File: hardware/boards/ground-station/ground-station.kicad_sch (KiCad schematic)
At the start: 10 parts, among them J101 Raspberry_Pi_2_3, J102 Conn_01x15, J5 Conn_01x12

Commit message: Added footprints for most things
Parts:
- J102: footprint (none) -> capstone:CON15_1X15_DRB_SFW; Part No. (none) -> SFW15R-1STE1LF
- J5: footprint (none) -> Connector_PinHeader_2.54mm:PinHeader_1x12_P2.54mm_Vertical
- R101, R102: footprint (none) -> Resistor_SMD:R_0201_0603Metric
- R23, R24, R25, R26: footprint (none) -> Resistor_SMD:R_0402_1005Metric
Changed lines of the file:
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@@
       (effects (font (size 1.27 1.27)))
     )
-    (property "Footprint" "" (at 220.98 122.555 0)
+    (property "Footprint" "Resistor_SMD:R_0402_1005Metric" (at 220.98 122.555 0)
       (effects (font (size 1.27 1.27)) hide)
     )
@@
       (effects (font (size 1.27 1.27)))
     )
-    (property "Footprint" "" (at 220.98 112.395 0)
+    (property "Footprint" "Resistor_SMD:R_0402_1005Metric" (at 220.98 112.395 0)
       (effects (font (size 1.27 1.27)) hide)
     )
@@
       (effects (font (size 1.27 1.27)) (justify left))
     )
-    (property "Footprint" "" (at 265.43 40.64 0)
+    (property "Footprint" "Connector_PinHeader_2.54mm:PinHeader_1x12_P2.54mm_Vertical" (at 265.43 40.64 0)
       (effects (font (size 1.27 1.27)) hide)
     )
     (property "Datasheet" "~" (at 265.43 40.64 0)
-      (effects (font (size 1.27 1.27)) hide)
-    )
-    (pin "5")
-    (pin "6")
-    (pin "7")
-    (pin "8")
-    (pin "1")
-    (pin "9")
-    (pin "3")
-    (pin "10")
-    (pin "11")
-    (pin "2")
-    (pin "12")
-    (pin "4")
-    (instances
-      (project "ground-station"
-        (path "/ce329892-de08-4d39-b253-15f3aaf1c085"
-          (reference "J5") (unit 1)
-        )
-      )
-    )
-  )
-  (symbol (lib_id "Device:R_Small_US") (at 128.905 34.29 180) (unit 1)
-    (in_bom yes) (on_board yes) (dnp no) (fields_autoplaced)
-    (property "Reference" "R102" (at 131.445 33.02 0)
-      (effects (font (size 1.27 1.27)) (justify right))
-    )
-    (property "Value" "4.7k" (at 131.445 35.56 0)
-      (effects (font (size 1.27 1.27)) (justify right))
-    )
-    (property "Footprint" "" (at 128.905 34.29 0)
-      (effects (font (size 1.27 1.27)) hide)
-    )
-    (property "Datasheet" "~" (at 128.905 34.29 0)
-      (effects (font (size 1.27 1.27)) hide)
-    )
-    (pin "1")
-    (pin "2")
-    (instances
-      (project "ground-station"
-        (path "/ce329892-de08-4d39-b253-15f3aaf1c085"
-          (reference "R102") (unit 1)
-        )
-      )
-    )
-  )
-  (symbol (lib_id "Device:R_Small_US") (at 120.015 34.29 180) (unit 1)
-    (in_bom yes) (on_board yes) (dnp no) (fields_autoplaced)
-    (property "Reference" "R101" (at 121.92 33.02 0)
-      (effects (font (size 1.27 1.27)) (justify right))
-    )
-    (property "Value" "4.7k" (at 121.92 35.56 0)
-      (effects (font (size 1.27 1.27)) (justify right))
-    )
-    (property "Footprint" "" (at 120.015 34.29 0)
-      (effects (font (size 1.27 1.27)) hide)
-    )
-    (property "Datasheet" "~" (at 120.015 34.29 0)
-      (effects (font (size 1.27 1.27)) hide)
-    )
-    (pin "1")
-    (pin "2")
-    (instances
-      (project "ground-station"
-        (path "/ce329892-de08-4d39-b253-15f3aaf1c085"
-          (reference "R101") (unit 1)
-        )
-      )
-    )
-  )
-  (symbol (lib_id "power:GND") (at 257.81 57.15 0) (unit 1)
-    (in_bom yes) (on_board yes) (dnp no)
-    (property "Reference" "#PWR06" (at 257.81 63.5 0)
-      (effects (font (size 1.27 1.27)) hide)
-    )
-    (property "Value" "GND" (at 257.81 60.96 0)
-      (effects (font (size 1.27 1.27)))
-    )
-    (property "Footprint" "" (at 257.81 57.15 0)
-      (effects (font (size 1.27 1.27)) hide)
-    )
-    (property "Datasheet" "" (at 257.81 57.15 0)
-      (effects (font (size 1.27 1.27)) hide)
-    )
-    (pin "1")
-    (instances
-      (project "ground-station"
-        (path "/ce329892-de08-4d39-b253-15f3aaf1c085"
-          (reference "#PWR06") (unit 1)
-        )
-      )
-    )
-  )
-  (symbol (lib_id "Device:R_Small") (at 220.98 114.935 90) (unit 1)
-    (in_bom yes) (on_board yes) (dnp no)
-    (property "Reference" "R26" (at 217.805 114.3 90)
-      (effects (font (size 1.27 1.27)))
-    )
-    (property "Value" "0" (at 223.52 114.3 90)
-      (effects (font (size 1.27 1.27)))
-    )
-    (property "Footprint" "" (at 220.98 114.935 0)
-      (effects (font (size 1.27 1.27)) hide)
-    )
-    (property "Datasheet" "~" (at 220.98 114.935 0)
-      (effects (font (size 1.27 1.27)) hide)
-    )
-    (pin "1")
-    (pin "2")
-    (instances
-      (project "ground-station"
-        (path "/ce329892-de08-4d39-b253-15f3aaf1c085"
-          (reference "R26") (unit 1)
-        )
-      )
-    )
-  )
-  (symbol (lib_id "Connector_Generic:Conn_01x15") (at 245.745 127.635 0) (unit 1)
-    (in_bom yes) (on_board yes) (dnp no) (fields_autoplaced)
-    (property "Reference" "J102" (at 245.745 103.505 0)
-      (effects (font (size 1.27 1.27)))
-    )
-    (property "Value" "Conn_01x15" (at 245.745 106.045 0)
-      (effects (font (size 1.27 1.27)))
-    )
-    (property "Footprint" "" (at 245.745 127.635 0)
-      (effects (font (size 1.27 1.27)) hide)
-    )
-    (property "Datasheet" "~" (at 245.745 127.635 0)
       (effects (font (size 1.27 1.27)) hide)
     )
@@
     (pin "11")
     (pin "12")
-    (pin "13")
-    (pin "14")
-    (pin "15")
     (pin "2")
     (pin "3")
@@
       (project "ground-station"
         (path "/ce329892-de08-4d39-b253-15f3aaf1c085"
+          (reference "J5") (unit 1)
+        )
+      )
+    )
+  )
+  (symbol (lib_id "Device:R_Small_US") (at 128.905 34.29 180) (unit 1)
+    (in_bom yes) (on_board yes) (dnp no) (fields_autoplaced)
+    (property "Reference" "R102" (at 131.445 33.02 0)
+      (effects (font (size 1.27 1.27)) (justify right))
+    )
+    (property "Value" "4.7k" (at 131.445 35.56 0)
+      (effects (font (size 1.27 1.27)) (justify right))
+    )
+    (property "Footprint" "Resistor_SMD:R_0201_0603Metric" (at 128.905 34.29 0)
+      (effects (font (size 1.27 1.27)) hide)
+    )
+    (property "Datasheet" "~" (at 128.905 34.29 0)
+      (effects (font (size 1.27 1.27)) hide)
+    )
+    (pin "1")
+    (pin "2")
+    (instances
+      (project "ground-station"
+        (path "/ce329892-de08-4d39-b253-15f3aaf1c085"
+          (reference "R102") (unit 1)
+        )
+      )
+    )
+  )
+  (symbol (lib_id "Device:R_Small_US") (at 120.015 34.29 180) (unit 1)
+    (in_bom yes) (on_board yes) (dnp no) (fields_autoplaced)
+    (property "Reference" "R101" (at 121.92 33.02 0)
+      (effects (font (size 1.27 1.27)) (justify right))
+    )
+    (property "Value" "4.7k" (at 121.92 35.56 0)
+      (effects (font (size 1.27 1.27)) (justify right))
+    )
+    (property "Footprint" "Resistor_SMD:R_0201_0603Metric" (at 120.015 34.29 0)
+      (effects (font (size 1.27 1.27)) hide)
+    )
+    (property "Datasheet" "~" (at 120.015 34.29 0)
+      (effects (font (size 1.27 1.27)) hide)
+    )
+    (pin "1")
+    (pin "2")
+    (instances
+      (project "ground-station"
+        (path "/ce329892-de08-4d39-b253-15f3aaf1c085"
+          (reference "R101") (unit 1)
+        )
+      )
+    )
+  )
+  (symbol (lib_id "power:GND") (at 257.81 57.15 0) (unit 1)
+    (in_bom yes) (on_board yes) (dnp no)
+    (property "Reference" "#PWR06" (at 257.81 63.5 0)
+      (effects (font (size 1.27 1.27)) hide)
+    )
+    (property "Value" "GND" (at 257.81 60.96 0)
+      (effects (font (size 1.27 1.27)))
+    )
+    (property "Footprint" "" (at 257.81 57.15 0)
+      (effects (font (size 1.27 1.27)) hide)
+    )
+    (property "Datasheet" "" (at 257.81 57.15 0)
+      (effects (font (size 1.27 1.27)) hide)
+    )
+    (pin "1")
+    (instances
+      (project "ground-station"
+        (path "/ce329892-de08-4d39-b253-15f3aaf1c085"
+          (reference "#PWR06") (unit 1)
+        )
+      )
+    )
+  )
+  (symbol (lib_id "Device:R_Small") (at 220.98 114.935 90) (unit 1)
+    (in_bom yes) (on_board yes) (dnp no)
+    (property "Reference" "R26" (at 217.805 114.3 90)
+      (effects (font (size 1.27 1.27)))
+    )
+    (property "Value" "0" (at 223.52 114.3 90)
+      (effects (font (size 1.27 1.27)))
+    )
+    (property "Footprint" "Resistor_SMD:R_0402_1005Metric" (at 220.98 114.935 0)
+      (effects (font (size 1.27 1.27)) hide)
+    )
+    (property "Datasheet" "~" (at 220.98 114.935 0)
+      (effects (font (size 1.27 1.27)) hide)
+    )
+    (pin "1")
+    (pin "2")
+    (instances
+      (project "ground-station"
+        (path "/ce329892-de08-4d39-b253-15f3aaf1c085"
+          (reference "R26") (unit 1)
+        )
+      )
+    )
+  )
+  (symbol (lib_id "Connector_Generic:Conn_01x15") (at 245.745 127.635 0) (unit 1)
+    (in_bom yes) (on_board yes) (dnp no) (fields_autoplaced)
+    (property "Reference" "J102" (at 245.745 103.505 0)
+      (effects (font (size 1.27 1.27)))
+    )
+    (property "Value" "Conn_01x15" (at 245.745 106.045 0)
+      (effects (font (size 1.27 1.27)))
+    )
+    (property "Footprint" "capstone:CON15_1X15_DRB_SFW" (at 245.745 127.635 0)
+      (effects (font (size 1.27 1.27)) hide)
+    )
+    (property "Datasheet" "https://cdn.amphenol-cs.com/media/wysiwyg/files/drawing/sfw12lf.pdf" (at 245.745 127.635 0)
+      (effects (font (size 1.27 1.27)) hide)
+    )
+    (property "Part No." "SFW15R-1STE1LF" (at 245.745 127.635 0)
+      (effects (font (size 1.27 1.27)) hide)
+    )
+    (pin "1")
+    (pin "10")
+    (pin "11")
+    (pin "12")
+    (pin "13")
+    (pin "14")
+    (pin "15")
+    (pin "2")
+    (pin "3")
+    (pin "4")
+    (pin "5")
+    (pin "6")
+    (pin "7")
+    (pin "8")
+    (pin "9")
+    (instances
+      (project "ground-station"
+        (path "/ce329892-de08-4d39-b253-15f3aaf1c085"
           (reference "J102") (unit 1)
         )
@@
       (effects (font (size 1.27 1.27)) hide)
     )
-    (pin "2")
-    (pin "1")
+    (pin "1")
+    (pin "2")
     (instances
       (project "ground-station"
@@
       (effects (font (size 1.27 1.27)))
     )
-    (property "Footprint" "" (at 220.98 120.015 0)
-      (effects (font (size 1.27 1.27)) hide)
-    )
+    (property "Footprint" "Resistor_SMD:R_0402_1005Metric" (at 220.98 120.015 0)
+      (effects (font (size 1.27 1.27)) hide)
+    )

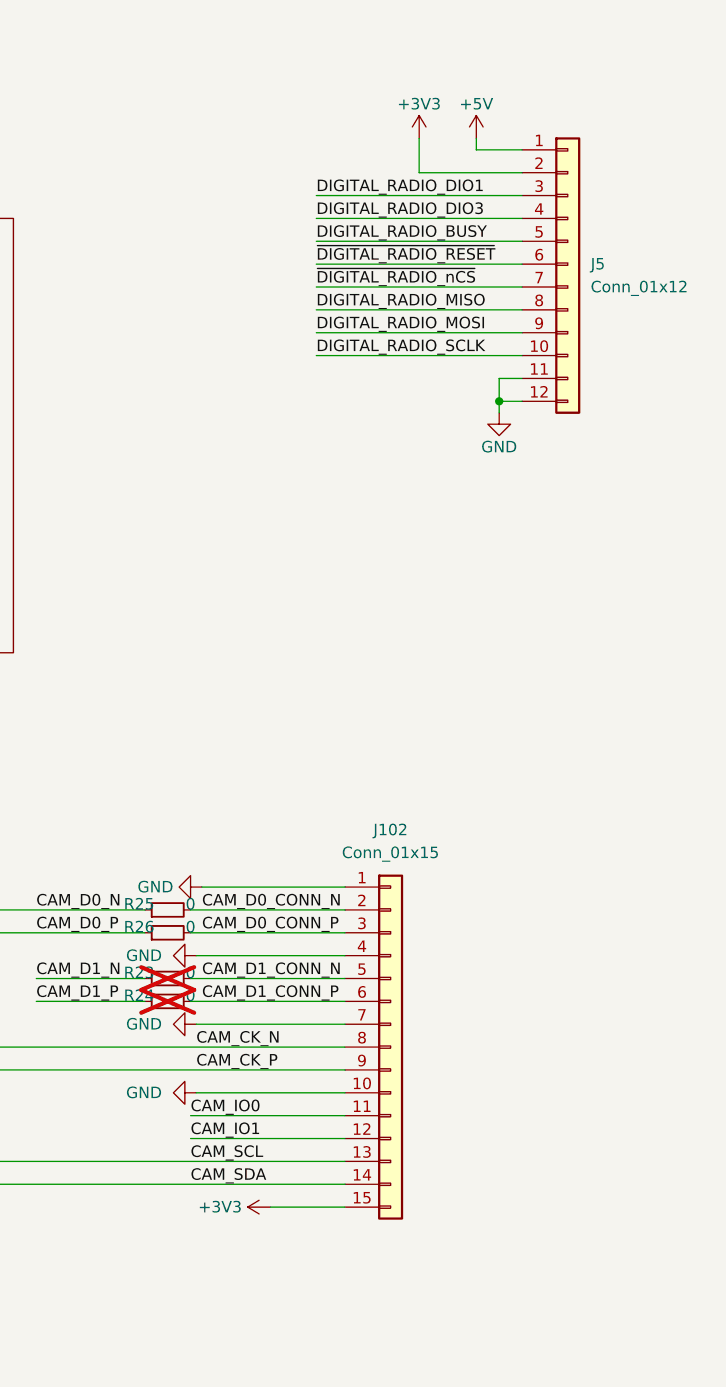
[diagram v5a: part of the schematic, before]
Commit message: Removed 10 pin radio header and changed ribbon cable connector
- disconnected 3V3 from the ribbon cable connector to keep the Pi 3V3 rail separate from the board 3V3 rail
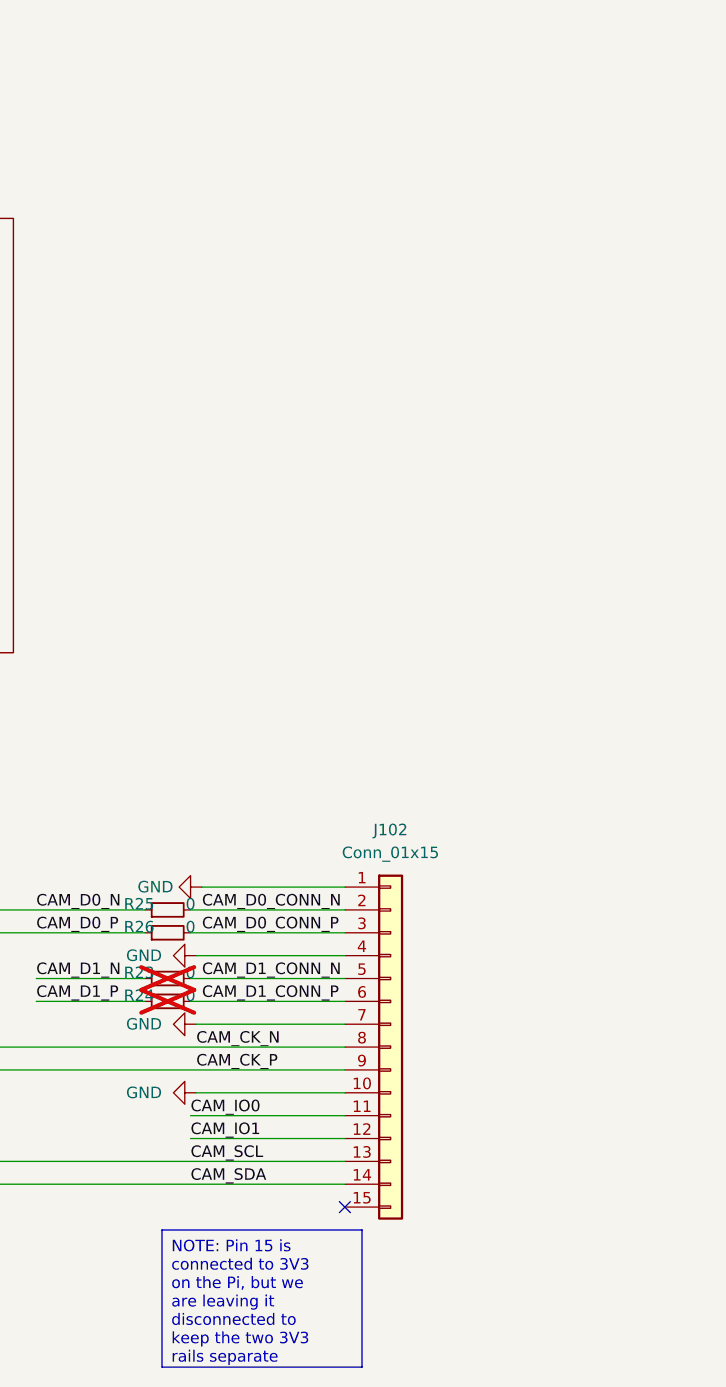
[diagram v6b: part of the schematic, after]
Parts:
- removed J5: Conn_01x12, Connector_PinHeader_2.54mm:PinHeader_1x12_P2.54mm_Vertical, symbol Connector_Generic:Conn_01x12
- J102: footprint capstone:CON15_1X15_DRB_SFW -> capstone:FFC3A20-15-G; Part No. SFW15R-1STE1LF -> FFC3A20-15-G
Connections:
- net +3V3: no longer J102.15 (Pin_15)
- no-connect marks 2 -> 3

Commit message: layout
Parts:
- removed R101, R102: 4.7k, Resistor_SMD:R_0201_0603Metric, symbol Device:R_Small_US
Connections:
- net CAM_D1_N is gone; now on net CAM_D0_N: R23.1
- net CAM_D1_P is gone; now on net CAM_D0_P: R24.1
- net I2C_SCL: no longer names the net of J101.5 (SCL/GPIO3)
- net I2C_SDA: no longer names the net of J101.3 (SDA/GPIO2)
- no-connect marks 3 -> 7
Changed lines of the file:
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@@
   (junction (at 79.375 91.44) (diameter 0) (color 0 0 0 0)
   )
+  (junction (at 205.105 112.395) (diameter 0) (color 0 0 0 0)
+  )
+  (junction (at 202.565 114.935) (diameter 0) (color 0 0 0 0)
+  )
   (junction (at 84.455 91.44) (diameter 0) (color 0 0 0 0)
   )
@@
   (junction (at 89.535 91.44) (diameter 0) (color 0 0 0 0)
   )
-  (junction (at 124.46 26.67) (diameter 0) (color 0 0 0 0)
-  )
   (junction (at 86.995 91.44) (diameter 0) (color 0 0 0 0)
   )
+  (no_connect (at 104.775 43.815))
   (no_connect (at 89.535 23.495))
+  (no_connect (at 104.775 41.275))
   (no_connect (at 86.995 23.495))
   (no_connect (at 240.665 145.415))
+  (no_connect (at 104.775 33.655))
+  (no_connect (at 104.775 36.195))
   (wire (pts (xy 86.995 91.44) (xy 84.455 91.44))
     (stroke (width 0) (type default))
@@
     (stroke (width 0) (type default))
   )
-  (wire (pts (xy 120.015 31.75) (xy 120.015 26.67))
-    (stroke (width 0) (type default))
-  )
-  (wire (pts (xy 104.775 43.815) (xy 128.905 43.815))
-    (stroke (width 0) (type default))
-  )
   (wire (pts (xy 45.085 64.135) (xy 64.135 64.135))
     (stroke (width 0) (type default))
@@
     (stroke (width 0) (type default))
   )
+  (wire (pts (xy 205.105 112.395) (xy 218.44 112.395))
+    (stroke (width 0) (type default))
+  )
   (wire (pts (xy 166.37 130.175) (xy 240.665 130.175))
     (stroke (width 0) (type default))
@@
     (stroke (width 0) (type default))
   )
-  (wire (pts (xy 197.485 112.395) (xy 218.44 112.395))
+  (wire (pts (xy 197.485 112.395) (xy 205.105 112.395))
     (stroke (width 0) (type default))
   )
@@
     (stroke (width 0) (type default))
   )
-  (wire (pts (xy 120.015 41.275) (xy 104.775 41.275))
-    (stroke (width 0) (type default))
-  )
   (wire (pts (xy 81.915 89.535) (xy 81.915 91.44))
     (stroke (width 0) (type default))
@@
     (stroke (width 0) (type default))
   )
-  (wire (pts (xy 218.44 120.015) (xy 206.375 120.015))
+  (wire (pts (xy 205.105 120.015) (xy 218.44 120.015))
     (stroke (width 0) (type default))
   )
@@
     (stroke (width 0) (type default))
   )
+  (wire (pts (xy 202.565 114.935) (xy 218.44 114.935))
+    (stroke (width 0) (type default))
+  )
   (wire (pts (xy 240.665 132.715) (xy 224.155 132.715))
     (stroke (width 0) (type default))
   )
-  (wire (pts (xy 218.44 122.555) (xy 206.375 122.555))
+  (wire (pts (xy 202.565 122.555) (xy 218.44 122.555))
     (stroke (width 0) (type default))
   )
@@
     (stroke (width 0) (type default))
   )
-  (wire (pts (xy 197.485 114.935) (xy 218.44 114.935))
+  (wire (pts (xy 197.485 114.935) (xy 202.565 114.935))
     (stroke (width 0) (type default))
   )
@@
     (stroke (width 0) (type default))
   )
-  (wire (pts (xy 128.905 31.75) (xy 128.905 26.67))
-    (stroke (width 0) (type default))
-  )
   (wire (pts (xy 240.665 125.095) (xy 224.155 125.095))
     (stroke (width 0) (type default))
@@
     (stroke (width 0) (type default))
   )
+  (wire (pts (xy 202.565 122.555) (xy 202.565 114.935))
+    (stroke (width 0) (type default))
+  )
   (wire (pts (xy 50.165 36.195) (xy 64.135 36.195))
     (stroke (width 0) (type default))
@@
     (stroke (width 0) (type default))
   )
-  (wire (pts (xy 120.015 36.83) (xy 120.015 41.275))
-    (stroke (width 0) (type default))
-  )
   (wire (pts (xy 156.21 140.335) (xy 240.665 140.335))
     (stroke (width 0) (type default))
   )
-  (wire (pts (xy 128.905 26.67) (xy 124.46 26.67))
-    (stroke (width 0) (type default))
-  )
   (wire (pts (xy 72.39 21.59) (xy 68.58 21.59))
     (stroke (width 0) (type default))
@@
     (stroke (width 0) (type default))
   )
+  (wire (pts (xy 205.105 120.015) (xy 205.105 112.395))
+    (stroke (width 0) (type default))
+  )
   (wire (pts (xy 86.995 89.535) (xy 86.995 91.44))
     (stroke (width 0) (type default))
@@
     (stroke (width 0) (type default))
   )
-  (wire (pts (xy 120.015 26.67) (xy 124.46 26.67))
-    (stroke (width 0) (type default))
-  )
   (wire (pts (xy 170.815 97.79) (xy 123.825 97.79))
     (stroke (width 0) (type default))
@@
   )
   (wire (pts (xy 81.915 23.495) (xy 81.915 21.59))
-    (stroke (width 0) (type default))
-  )
-  (wire (pts (xy 128.905 43.815) (xy 128.905 36.83))
     (stroke (width 0) (type default))
   )
@@
     (effects (font (size 1.27 1.27)) (justify left bottom))
   )
-  (label "I2C_SCL" (at 107.315 43.815 0) (fields_autoplaced)
-    (effects (font (size 1.27 1.27)) (justify left bottom))
-  )
-  (label "CAM_D1_P" (at 206.375 122.555 0) (fields_autoplaced)
-    (effects (font (size 1.27 1.27)) (justify left bottom))
-  )
   (label "CAM_D1_CONN_P" (at 224.79 122.555 0) (fields_autoplaced)
     (effects (font (size 1.27 1.27)) (justify left bottom))
@@
     (effects (font (size 1.27 1.27)) (justify left bottom))
   )
-  (label "CAM_D1_N" (at 206.375 120.015 0) (fields_autoplaced)
-    (effects (font (size 1.27 1.27)) (justify left bottom))
-  )
   (label "~{DIGITIZER_RESET}" (at 151.765 105.41 0) (fields_autoplaced)
     (effects (font (size 1.27 1.27)) (justify left bottom))
   )
   (label "GPS_UART_TX" (at 157.48 41.275 0) (fields_autoplaced)
-    (effects (font (size 1.27 1.27)) (justify left bottom))
-  )
-  (label "I2C_SDA" (at 107.315 41.275 0) (fields_autoplaced)
     (effects (font (size 1.27 1.27)) (justify left bottom))
   )
@@
     )
   )
-  (symbol (lib_id "power:+3V3") (at 124.46 26.67 0) (unit 1)
-    (in_bom yes) (on_board yes) (dnp no) (fields_autoplaced)
-    (property "Reference" "#PWR0101" (at 124.46 30.48 0)
-      (effects (font (size 1.27 1.27)) hide)
-    )
-    (property "Value" "+3V3" (at 124.46 21.59 0)
-      (effects (font (size 1.27 1.27)))
-    )
-    (property "Footprint" "" (at 124.46 26.67 0)
-      (effects (font (size 1.27 1.27)) hide)
-    )
-    (property "Datasheet" "" (at 124.46 26.67 0)
-      (effects (font (size 1.27 1.27)) hide)
-    )
-    (pin "1")
-    (instances
-      (project "ground-station"
-        (path "/ce329892-de08-4d39-b253-15f3aaf1c085"
-          (reference "#PWR0101") (unit 1)
-        )
-      )
-    )
-  )
   (symbol (lib_id "power:+5V") (at 68.58 18.415 0) (unit 1)
     (in_bom yes) (on_board yes) (dnp no)
@@
         )
       )
-    )
-  )
-  (symbol (lib_id "Device:R_Small_US") (at 128.905 34.29 180) (unit 1)
-    (in_bom yes) (on_board yes) (dnp no) (fields_autoplaced)
-    (property "Reference" "R102" (at 131.445 33.02 0)
-      (effects (font (size 1.27 1.27)) (justify right))
-    )
-    (property "Value" "4.7k" (at 131.445 35.56 0)
-      (effects (font (size 1.27 1.27)) (justify right))
-    )
-    (property "Footprint" "Resistor_SMD:R_0201_0603Metric" (at 128.905 34.29 0)
-      (effects (font (size 1.27 1.27)) hide)
-    )
-    (property "Datasheet" "~" (at 128.905 34.29 0)
-      (effects (font (size 1.27 1.27)) hide)
-    )
-    (pin "1")
-    (pin "2")
-    (instances
-      (project "ground-station"
-        (path "/ce329892-de08-4d39-b253-15f3aaf1c085"
-          (reference "R102") (unit 1)
-        )
-      )
-    )
-  )
-  (symbol (lib_id "Device:R_Small_US") (at 120.015 34.29 180) (unit 1)
-    (in_bom yes) (on_board yes) (dnp no) (fields_autoplaced)
-    (property "Reference" "R101" (at 121.92 33.02 0)
-      (effects (font (size 1.27 1.27)) (justify right))
-    )
-    (property "Value" "4.7k" (at 121.92 35.56 0)
-      (effects (font (size 1.27 1.27)) (justify right))
-    )
-    (property "Footprint" "Resistor_SMD:R_0201_0603Metric" (at 120.015 34.29 0)
-      (effects (font (size 1.27 1.27)) hide)
-    )
-    (property "Datasheet" "~" (at 120.015 34.29 0)
-      (effects (font (size 1.27 1.27)) hide)
-    )
-    (pin "1")
-    (pin "2")
-    (instances
-      (project "ground-station"
-        (path "/ce329892-de08-4d39-b253-15f3aaf1c085"
-          (reference "R101") (unit 1)
-        )
-      )
